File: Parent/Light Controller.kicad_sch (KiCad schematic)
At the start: 23 parts, among them J10 Screw_Terminal_01x04, J12 Screw_Terminal_01x07, J9 Screw_Terminal_01x04, Q3 FQP27P06, Q4 FQP27P06, Q5 FQP27P06, Q6 FQP27P06, Q7 FQP27P06, U3 NSL-32, U35 NSL-32, U4 NSL-32, U5 NSL-32, U6 NSL-32

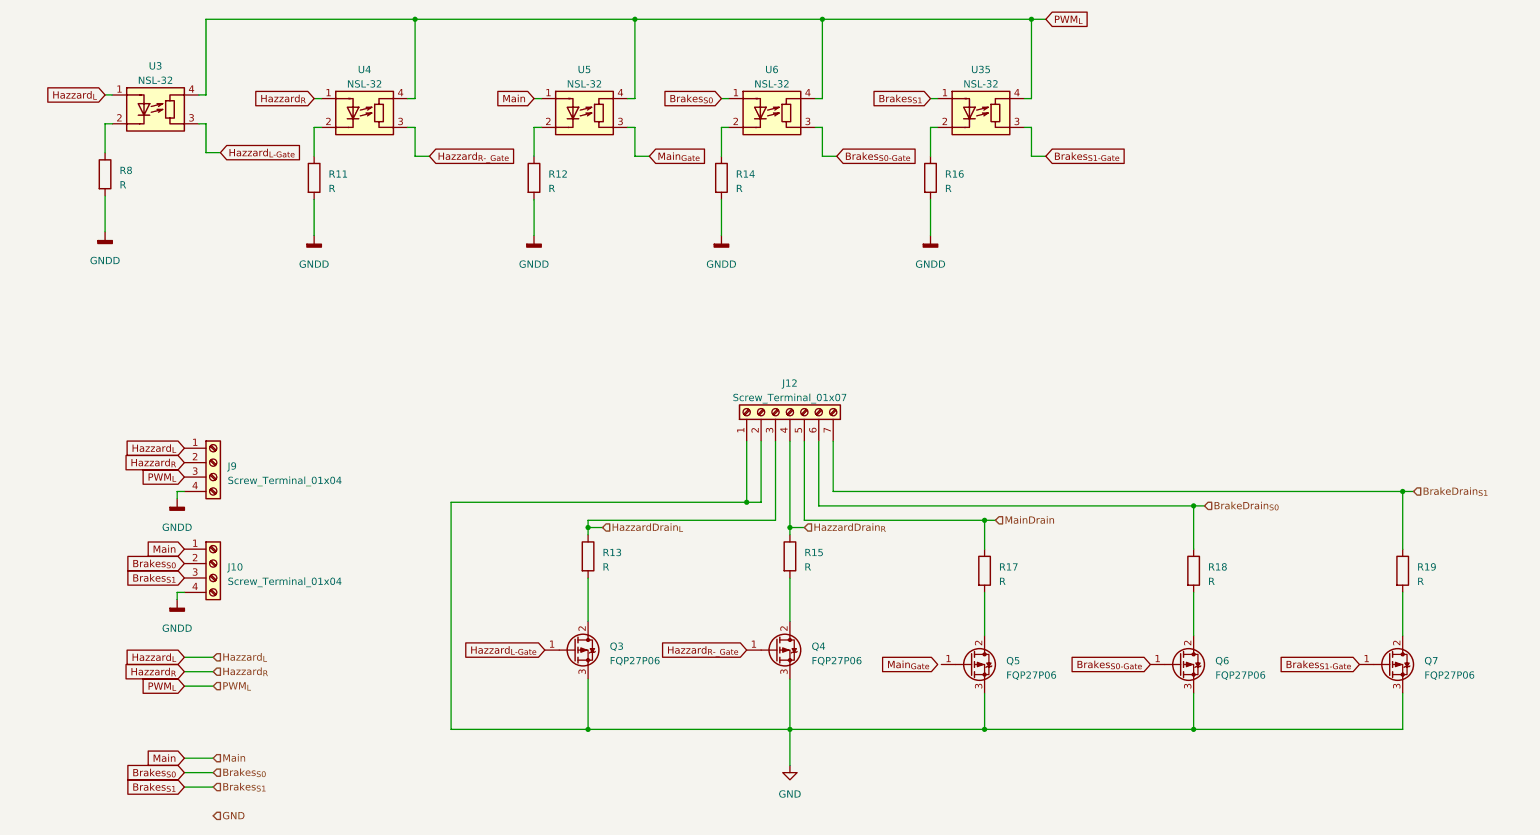
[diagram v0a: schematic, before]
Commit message: Updated Parent - Moved workspace to cloud
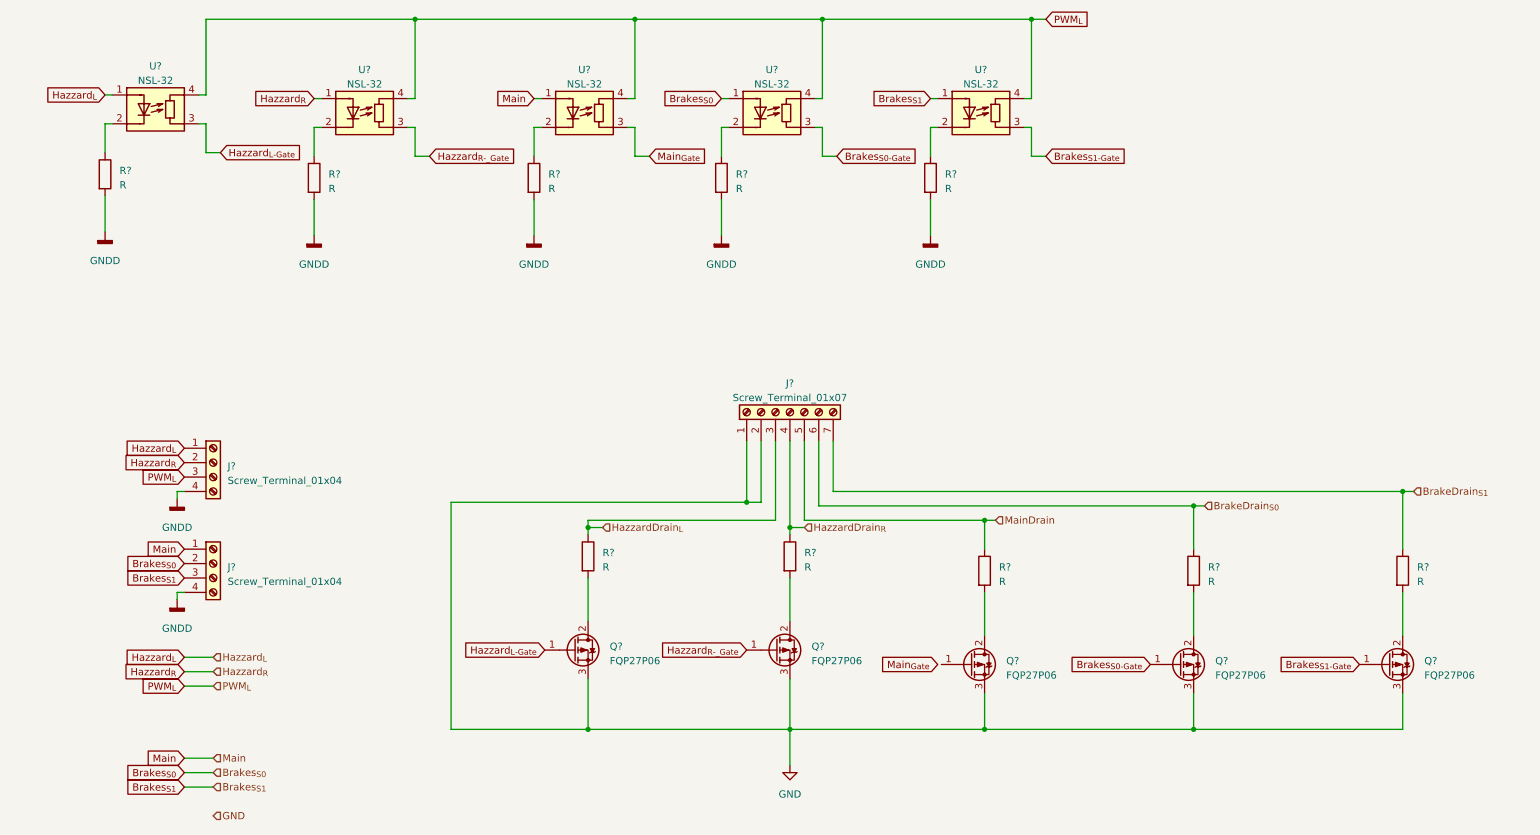
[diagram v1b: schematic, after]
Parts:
- renumbered J9 to J?, J12 to J?, J10 to J?, Q4 to Q?, Q6 to Q?, Q7 to Q?, Q3 to Q?, Q5 to Q?, R13 to R?, R18 to R?, R19 to R?, R15 to R?, R12 to R?, R17 to R?, R14 to R?, R16 to R?, R8 to R?, R11 to R?, U4 to U?, U3 to U?, U5 to U?, U35 to U?, U6 to U?
